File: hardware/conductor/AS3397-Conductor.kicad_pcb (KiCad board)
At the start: 2 copper layers, 36 parts, among them J1 ES, J10 MIDI IN, J11 POWER, J2 ES, J3 ES, J4 ES, J8 ES, J9 AudioJack3, Q1 BS170F, U1 TL072, U3 6N138

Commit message: Conductor board new version
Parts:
- removed Q1: BS170F, Package_TO_SOT_SMD:SOT-23
- removed R11, R15, R16, R4, R5, R6, R7, R8: R, Resistor_THT:R_Axial_DIN0204_L3.6mm_D1.6mm_P7.62mm_Horizontal
- removed R17: 4k7, Resistor_THT:R_Axial_DIN0204_L3.6mm_D1.6mm_P7.62mm_Horizontal
- removed U1: TL072, Package_DIP:DIP-8_W7.62mm_LongPads
- added A1: SC0918, picoW:MODULE_SC0918, F.Cu at (153.4, 126.7)
- added C3: 100n, Capacitor_SMD:C_1206_3216Metric_Pad1.33x1.80mm_HandSolder, F.Cu at (116.8, 71.6)
- added C4: 100n, Capacitor_SMD:C_1206_3216Metric_Pad1.33x1.80mm_HandSolder, F.Cu at (129.7, 71.6)
- added C5: 100n, Capacitor_SMD:C_1206_3216Metric_Pad1.33x1.80mm_HandSolder, F.Cu at (182.6, 123.3)
- added C6: 120pF, Capacitor_SMD:C_1206_3216Metric_Pad1.33x1.80mm_HandSolder, F.Cu at (128.4, 67.9)
- added C7: 120pF, Capacitor_SMD:C_1206_3216Metric_Pad1.33x1.80mm_HandSolder, F.Cu at (118.1, 67.8)
- added D2: LED, Diode_THT:D_A-405_P2.54mm_Vertical_AnodeUp, F.Cu at (196.2, 149.3)
- added D3: 1N5819, Diode_THT:D_DO-41_SOD81_P10.16mm_Horizontal, F.Cu at (138.0, 151.9)
- added J12: Conn_01x03_Socket_AudioOUT, Connector_JST:JST_EH_B3B-EH-A_1x03_P2.50mm_Vertical, F.Cu at (155.8, 81.0)
- added J13: Voice connector, Connector_JST:JST_EH_B9B-EH-A_1x09_P2.50mm_Vertical, F.Cu at (114.0, 101.1)
- added J14: Conn_01x02_Socket, Connector_JST:JST_EH_B2B-EH-A_1x02_P2.50mm_Vertical, F.Cu at (176.0, 83.1)
- added J15: I2C controller, Connector_JST:JST_EH_B4B-EH-A_1x04_P2.50mm_Vertical, F.Cu at (167.0, 95.4)
- added J16: Conn_01x06_Socket_SPI, Connector_PinSocket_2.54mm:PinSocket_1x06_P2.54mm_Vertical, F.Cu at (168.1, 135.7)
- added J17: Conn_01x03_Socket, Connector_PinHeader_2.54mm:PinHeader_1x03_P2.54mm_Vertical, F.Cu at (168.2, 140.3)
- added J18: Conn_01x03_Socket, Connector_PinHeader_2.54mm:PinHeader_1x03_P2.54mm_Vertical, F.Cu at (179.9, 102.3)
- added J5: Conn_01x02_Socket, Connector_JST:JST_EH_B2B-EH-A_1x02_P2.50mm_Vertical, F.Cu at (189.3, 140.6)
- added J6: AudioJack3, Connector_Audio:Jack_3.5mm_Ledino_KB3SPRS_Horizontal, F.Cu at (148.0, 66.0)
- added J7: Conn_POWER, Connector_PinHeader_2.54mm:PinHeader_2x05_P2.54mm_Vertical, F.Cu at (115.1, 148.7)
- added R26: 5K1, Resistor_SMD:R_1206_3216Metric_Pad1.30x1.75mm_HandSolder, F.Cu at (125.8, 64.4)
- added R27: 4K7, Resistor_SMD:R_1206_3216Metric_Pad1.30x1.75mm_HandSolder, F.Cu at (119.0, 108.8)
- added R28: 4K7, Resistor_SMD:R_1206_3216Metric_Pad1.30x1.75mm_HandSolder, F.Cu at (118.9, 106.2)
- added R29: 4K7, Resistor_SMD:R_1206_3216Metric_Pad1.30x1.75mm_HandSolder, F.Cu at (166.9, 101.2)
- added R30: 4K7, Resistor_SMD:R_1206_3216Metric_Pad1.30x1.75mm_HandSolder, F.Cu at (166.8, 89.5)
- added U2: 6N138, Package_DIP:DIP-8_W7.62mm_LongPads, F.Cu at (189.9, 66.1)
- C1, C2: footprint Capacitor_THT:C_Disc_D4.3mm_W1.9mm_P5.00mm -> Capacitor_SMD:C_1206_3216Metric_Pad1.33x1.80mm_HandSolder
- J1: value ES -> Micro_SD_Card; footprint SYNTHFILLE:DIP-16_AS -> SD_card:J_SD_Card-micro_socket_A
- J10: value MIDI IN -> Conn_FX_2; footprint lib:MIDI_DIN5 -> Connector_PinHeader_2.54mm:PinHeader_2x05_P2.54mm_Vertical
- J11: value POWER -> I2C controller; footprint TerminalBlock:TerminalBlock_bornier-4_P5.08mm -> Connector_JST:JST_EH_B4B-EH-A_1x04_P2.50mm_Vertical
- J2: value ES -> ADC_connector; footprint SYNTHFILLE:DIP-16_AS -> Connector_JST:JST_EH_B4B-EH-A_1x04_P2.50mm_Vertical
- J3: value ES -> Conn_01x06_Socket; footprint SYNTHFILLE:DIP-16_AS -> Connector_PinHeader_2.54mm:PinHeader_1x06_P2.54mm_Vertical
- J4: value ES -> I2C controller; footprint SYNTHFILLE:DIP-16_AS -> Connector_JST:JST_EH_B4B-EH-A_1x04_P2.50mm_Vertical
- J8: value ES -> MIDI IN; footprint SYNTHFILLE:DIP-16_AS -> Eurocad:MIDI_DIN5
- J9: value AudioJack3 -> Conn_FX_1; footprint Connector_Audio:Jack_3.5mm_Ledino_KB3SPRS_Horizontal -> Connector_PinHeader_2.54mm:PinHeader_2x05_P2.54mm_Vertical
- R1: value R -> 1K; footprint Resistor_THT:R_Axial_DIN0204_L3.6mm_D1.6mm_P7.62mm_Horizontal -> Resistor_SMD:R_1206_3216Metric_Pad1.30x1.75mm_HandSolder
- R10, R22, R23, R24, R25, R9: value R -> 10K; footprint Resistor_THT:R_Axial_DIN0204_L3.6mm_D1.6mm_P7.62mm_Horizontal -> Resistor_SMD:R_1206_3216Metric_Pad1.30x1.75mm_HandSolder
- R18: value 4k7 -> 220; footprint Resistor_THT:R_Axial_DIN0204_L3.6mm_D1.6mm_P7.62mm_Horizontal -> Resistor_SMD:R_1206_3216Metric_Pad1.30x1.75mm_HandSolder
- R19: value 220 -> 4k7; footprint Resistor_THT:R_Axial_DIN0204_L3.6mm_D1.6mm_P7.62mm_Horizontal -> Resistor_SMD:R_1206_3216Metric_Pad1.30x1.75mm_HandSolder
- R2, R3: value R -> 51; footprint Resistor_THT:R_Axial_DIN0204_L3.6mm_D1.6mm_P7.62mm_Horizontal -> Resistor_SMD:R_1206_3216Metric_Pad1.30x1.75mm_HandSolder
- R20: value 4k7 -> 470; footprint Resistor_THT:R_Axial_DIN0204_L3.6mm_D1.6mm_P7.62mm_Horizontal -> Resistor_SMD:R_1206_3216Metric_Pad1.30x1.75mm_HandSolder
- R21: value 470 -> 5K1; footprint Resistor_THT:R_Axial_DIN0204_L3.6mm_D1.6mm_P7.62mm_Horizontal -> Resistor_SMD:R_1206_3216Metric_Pad1.30x1.75mm_HandSolder
- U3: value 6N138 -> OPA1679; footprint Package_DIP:DIP-8_W7.62mm_LongPads -> Package_SO:SOIC-14_3.9x8.7mm_P1.27mm
- moved R3 215.8 mm to (191.8, 147.3)
- moved J1 213.3 mm to (194.8, 123.8), turned to -90 degrees
- moved J2 120.8 mm to (138.0, 128.2), turned to -90 degrees
- moved J9 118.3 mm to (134.3, 95.7), turned to -90 degrees
- moved R23 116.0 mm to (111.4, 71.7)
- moved C1 112.4 mm to (118.1, 75.5), turned to -90 degrees
- moved J4 109.5 mm to (149.4, 95.1)
- moved J10 98.4 mm to (134.2, 86.9), turned to -90 degrees
- moved R21 97.5 mm to (120.6, 64.3), turned to -90 degrees
- moved C2 95.7 mm to (128.4, 75.3), turned to -90 degrees
- moved R18 82.9 mm to (190.0, 78.1), turned to 0 degrees
- moved U3 73.4 mm to (123.3, 71.5)
- moved R9 72.5 mm to (130.8, 75.3), turned to -90 degrees
- moved R10 71.1 mm to (115.6, 75.5), turned to -90 degrees
- moved J8 67.2 mm to (177.0, 68.7), turned to 180 degrees
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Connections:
- C1 pad 1: Net-(U1A--) -> audio_analog_left
- C1 pad 2: Net-(C1-Pad2) -> Dry_left
- C2 pad 1: Net-(U1B--) -> audio_analog_right
- C2 pad 2: Net-(C2-Pad2) -> Dry_right
- J1 pad 1: Net-(J1-Pin_1) -> unconnected-(J1-DAT2-Pad1)
- J1 pad 2: I2C_SCK -> SD_CS
- J1 pad 3: I2C_SDA -> SD_MOSI
- J1 pad 4: +12V -> +3.3V
- J1 pad 5: GND -> SD_SCLK
- J1 pad 6: +5V -> GND
- J1 pad 7: Net-(J1-Pin_7) -> SD_MISO
- J1 pad 8: -5V -> unconnected-(J1-DAT1-Pad8)
- J1 pad 9: Net-(J1-Pin_9) -> GND
- J10 pad 1: unconnected-(J10-Pad1) -> Dry_left
- J10 pad 2: unconnected-(J10-Pad2) -> I2C_CTRL_SDL
- J10 pad 3: unconnected-(J10-Pad3) -> Wet_left
- J10 pad 4: Net-(J10-Pad4) -> I2C_CTRL_SDA
- J10 pad 5: Net-(D1-K) -> Dry_right
- J11 pad 1: GND -> I2C_CTRL_SDL
- J11 pad 2: -5V -> I2C_CTRL_SDA
- J11 pad 3: +5V -> +3.3V
- J11 pad 4: -12V -> GND
- J2 pad 1: Net-(J2-Pin_1) -> ADC0
- J2 pad 2: Net-(J1-Pin_15) -> ADC1
- J2 pad 3: Net-(J1-Pin_14) -> ADC2
- J2 pad 4: Net-(J1-Pin_13) -> GND
- J3 pad 1: Net-(J3-Pin_1) -> GND
- J3 pad 2: Net-(J2-Pin_15) -> GPIO18
- J3 pad 3: Net-(J2-Pin_14) -> GPIO19
- J3 pad 4: Net-(J2-Pin_13) -> GPIO20
- J3 pad 5: Net-(J2-Pin_12) -> GPIO21
- J3 pad 6: Net-(J2-Pin_11) -> GPIO22
- J4 pad 1: Net-(J4-Pin_1) -> I2C_CTRL_SDL
- J4 pad 2: Net-(J3-Pin_15) -> I2C_CTRL_SDA
- J4 pad 3: Net-(J3-Pin_14) -> +3.3V
- J4 pad 4: Net-(J3-Pin_13) -> GND
- J8 pad 1: Net-(J8-Pin_1) -> unconnected-(J8-Pad1)
- J8 pad 2: Net-(J4-Pin_15) -> unconnected-(J8-Pad2)
- J8 pad 3: Net-(J4-Pin_14) -> unconnected-(J8-Pad3)
- J8 pad 4: Net-(J4-Pin_13) -> Net-(J14-Pin_1)
- J8 pad 5: Net-(J4-Pin_12) -> Net-(D1-K)
- R1 pad 1: Net-(U1A--) -> TX_MIDI
- R1 pad 2: Net-(C1-Pad2) -> Net-(D2-K)
- R10 pad 1: Net-(U1B--) -> audio_analog_left
- R10 pad 2: Net-(J4-Pin_16) -> Dry_left
- R18 pad 1: +3.3V -> Net-(J14-Pin_1)
- R18 pad 2: I2C_SDA -> Net-(D1-A)
- R19 pad 1: Net-(J10-Pad4) -> Net-(U2-VO1)
- R19 pad 2: Net-(D1-A) -> GND
- R2 pad 1: Net-(U1B--) -> +3.3V
- R2 pad 2: Net-(C2-Pad2) -> Net-(J5-Pin_1)
- R20 pad 1: Net-(U3-VO1) -> +3.3V
- R20 pad 2: GND -> RX_MIDI
- R21 pad 1: +3.3V -> Net-(U3A--)
- R21 pad 2: RX -> Out_left
- R22 pad 1: Net-(J1-Pin_10) -> Dry_left
- R22 pad 2: Net-(J2-Pin_7) -> Net-(U3A--)
- R23 pad 1: Net-(J2-Pin_10) -> Wet_left
- R23 pad 2: Net-(J3-Pin_7) -> Net-(U3A--)
- R24 pad 1: Net-(J3-Pin_10) -> Dry_right
- R24 pad 2: Net-(J4-Pin_7) -> Net-(U3D--)
- R25 pad 1: Net-(J4-Pin_10) -> Wet_right
- R25 pad 2: Net-(J8-Pin_7) -> Net-(U3D--)
- R3 pad 1: Net-(U1A--) -> TX_MIDI
- R3 pad 2: Net-(J1-Pin_1) -> Net-(J5-Pin_2)
- R9 pad 1: Net-(U1A--) -> audio_analog_right
- R9 pad 2: Net-(J4-Pin_1) -> Dry_right
- U3 pad 1: unconnected-(U3-NC-Pad1) -> Out_left
- U3 pad 2: Net-(D1-K) -> Net-(U3A--)
- U3 pad 3: Net-(D1-A) -> GND
- U3 pad 4: unconnected-(U3-NC-Pad4) -> +5V
- U3 pad 6: RX -> audio_analog_left
- U3 pad 7: Net-(U3-VO1) -> Dry_left
- U3 pad 8: +5V -> Dry_right
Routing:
- net +5V: track 0.00 -> 263.4 mm, vias 0 -> 1
- net +3.3V: track 0.00 -> 235.6 mm, vias 0 -> 1
- net RX_MIDI: track 0.00 -> 131.0 mm
- net I2C_voices_SDL: track 0.00 -> 103.9 mm, vias 0 -> 2
- net -5V: track 0.00 -> 102.3 mm, vias 0 -> 3
- net I2C_voices_SDA: track 0.00 -> 96.0 mm, vias 0 -> 2
- net I2C_CTRL_SDA: track 0.00 -> 87.5 mm, vias 0 -> 2
- net +12V: track 0.00 -> 83.9 mm, vias 0 -> 1
- net Out_left: track 0.00 -> 74.5 mm
- net Dry_right: track 0.00 -> 59.1 mm, vias 0 -> 1
- net Wet_left: track 0.00 -> 58.1 mm, vias 0 -> 1
- net I2C_CTRL_SDL: track 0.00 -> 56.1 mm
- net Out_right: track 0.00 -> 52.8 mm
- net Dry_left: track 0.00 -> 49.8 mm, vias 0 -> 1
- net Wet_right: track 0.00 -> 43.8 mm, vias 0 -> 2
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- added copper zone on B.Cu, net GND
- added copper zone on F.Cu, net GND
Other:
- board outline added: 97.3 x 97.8 mm
- board text added: "-5V GND GND GND GND"
- board text added: "-> CTRL"
- board text added: "-> FX"
- board text added: "-> Voices"
- board text added: "22 21 20 19 18 GND"
- board text added: "4 sink"
- board text added: "5 source"
- board text added: "G R L"
- board text added: "GND +5V +12 GND GND"
- board text added: "GND 04 05"
- board text added: "GND 3V3 SCK TX RX CS"
- board text added: "GND ADC2 ADC1 ADC0"
- board text added: "L R SCL SDA 12 GND +5 ADD -5"
- board text added: "MIDI OUT"
- board text added: "Power"
- board text added: "SCL SDA 3V3 GND"

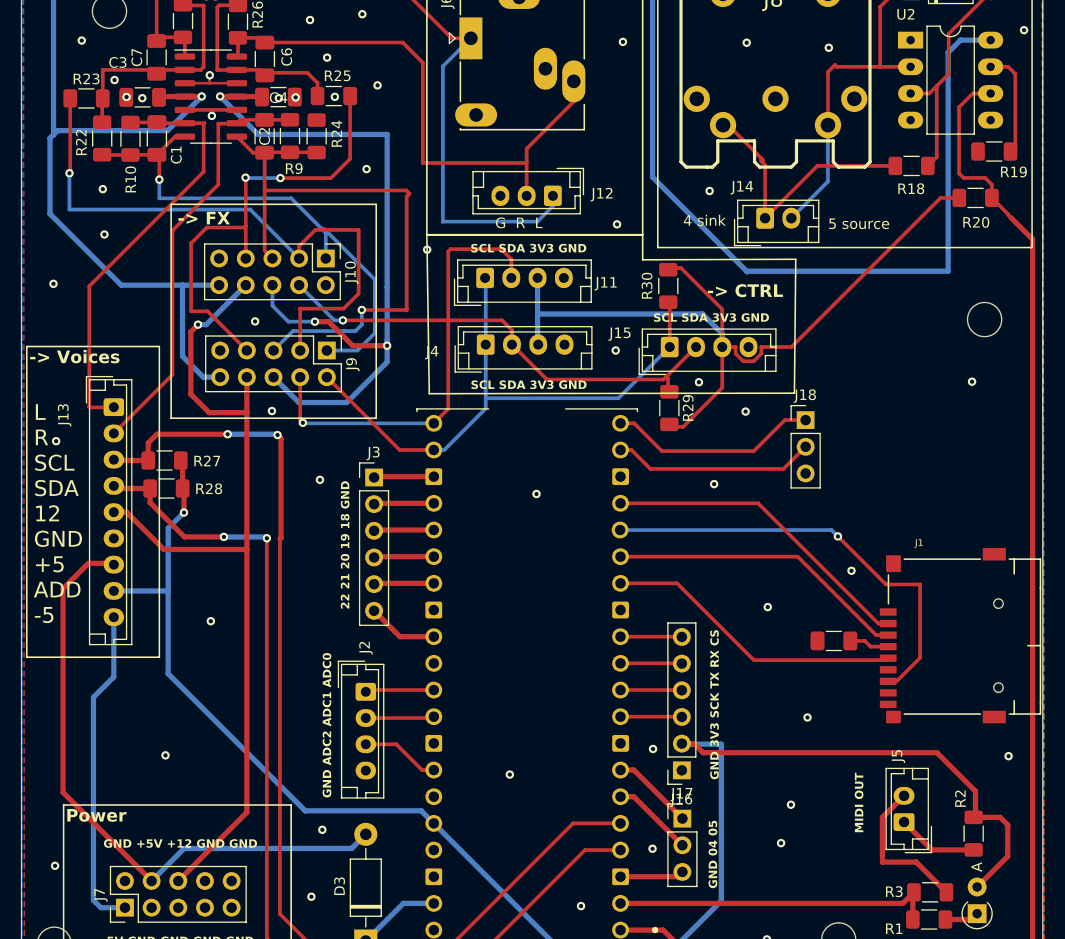
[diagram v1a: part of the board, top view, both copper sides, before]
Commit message: Fixing routing power rail in conductor board
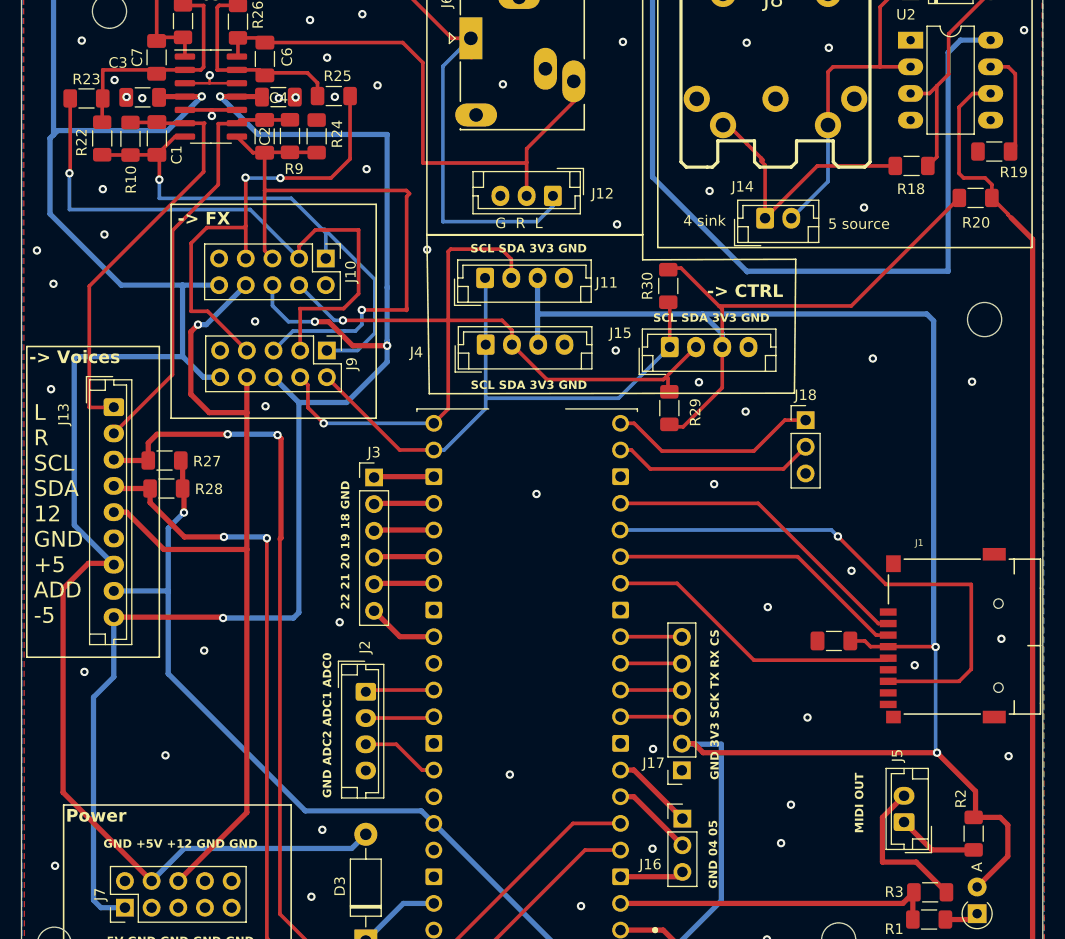
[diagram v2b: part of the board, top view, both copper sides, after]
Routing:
- net +3.3V: track 235.6 -> 300.6 mm, vias 1 -> 3
- net -5V: track 102.3 -> 140.2 mm, vias 3 -> 4
- net +5V: track 263.4 -> 295.1 mm
- net SD_MISO: track 41.7 -> 52.1 mm
- net I2C_CTRL_SDA: track 87.5 -> 86.4 mm
- net GND: vias 51 -> 58
